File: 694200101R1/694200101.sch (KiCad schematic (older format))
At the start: 226 parts, among them J1 USB4085-GF-A, J2 Conn_01x02_Male, J3 Conn_01x02_Male, SW1 MX_SW, SW10 MX_SW, SW100 MX_SW, SW101 MX_SW, SW102 MX_SW, SW11 MX_SW, SW12 MX_SW, SW13 MX_SW, SW14 MX_SW, SW15 MX_SW, SW16 MX_SW, SW17 MX_SW, SW18 MX_SW, SW19 MX_SW, SW2 MX_SW, SW20 MX_SW, SW21 MX_SW, SW22 MX_SW, SW23 MX_SW, SW24 MX_SW, SW25 MX_SW, SW26 MX_SW, SW27 MX_SW, SW28 MX_SW, SW29 MX_SW, SW3 MX_SW, SW30 MX_SW, SW31 MX_SW, SW32 MX_SW, SW33 MX_SW, SW34 MX_SW, SW35 MX_SW, SW36 MX_SW, SW37 MX_SW, SW38 MX_SW, SW39 MX_SW, SW4 MX_SW, SW40 MX_SW, SW41 MX_SW, SW42 MX_SW, SW43 MX_SW, SW44 MX_SW, SW45 MX_SW, SW46 MX_SW, SW47 MX_SW, SW48 MX_SW, SW49 MX_SW, SW5 MX_SW, SW50 MX_SW, SW51 MX_SW, SW52 MX_SW, SW53 MX_SW, SW54 MX_SW, SW55 MX_SW, SW56 MX_SW, SW57 MX_SW, SW58 MX_SW, SW59 MX_SW, SW6 MX_SW, SW60 MX_SW, SW61 MX_SW, SW62 MX_SW, SW63 MX_SW, SW64 MX_SW, SW65 MX_SW, SW66 MX_SW, SW67 MX_SW, SW68 MX_SW, SW69 MX_SW, SW7 MX_SW, SW70 MX_SW, SW71 MX_SW, SW72 MX_SW, SW73 MX_SW, SW74 MX_SW, SW75 MX_SW, SW76 MX_SW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

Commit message: Added Missing Col_8
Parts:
- added D? (x5): LL4148, eec-fairchild:Fairchild_ON_Semiconductor-LL4148-0, symbol eec-fairchild:LL4148
- added SW? (x5): MX_SW, cldg:millmax-mxalps, symbol cldg:MX_SW
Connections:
- wire segments 567 -> 582
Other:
- moved on the sheet: D100, D101, D102, D103, D40, D41, D42, D43, D44, D45, D46, D47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

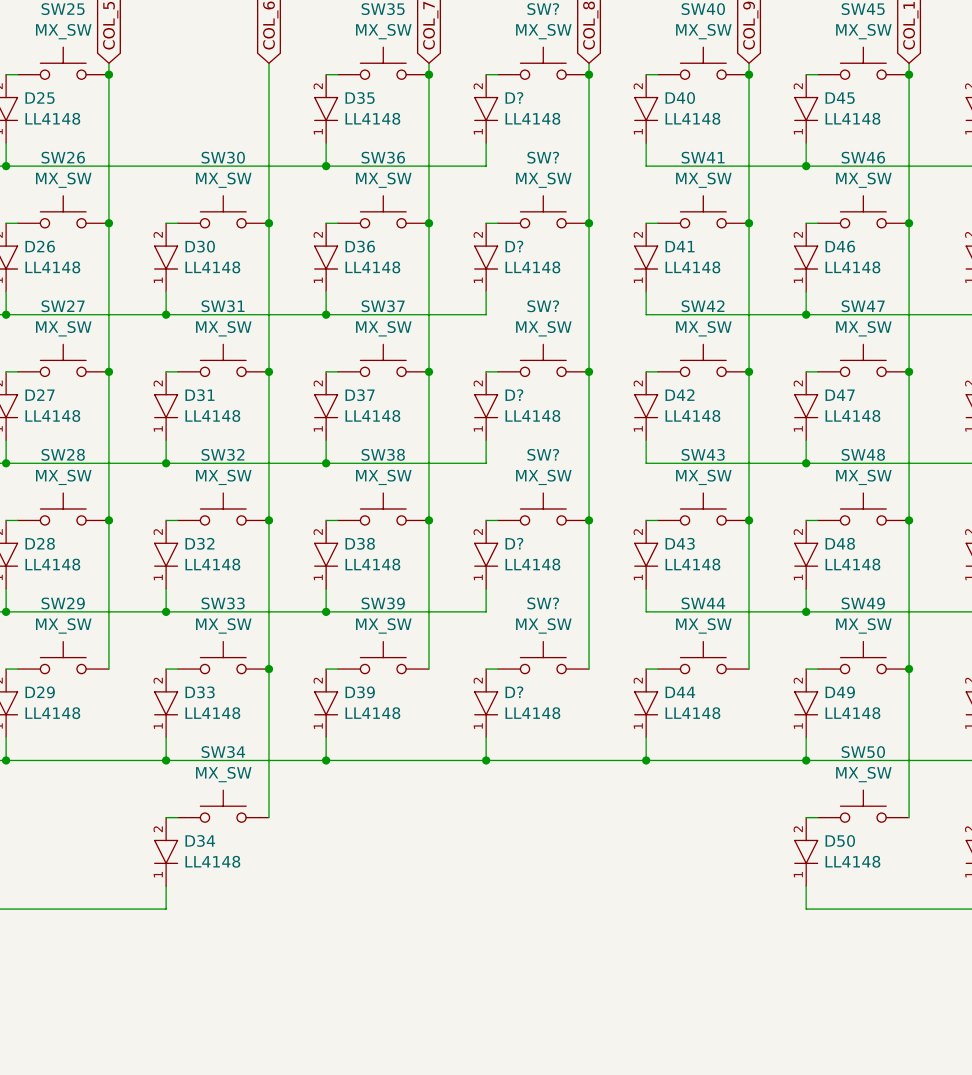
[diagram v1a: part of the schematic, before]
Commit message: Added Missing Wires
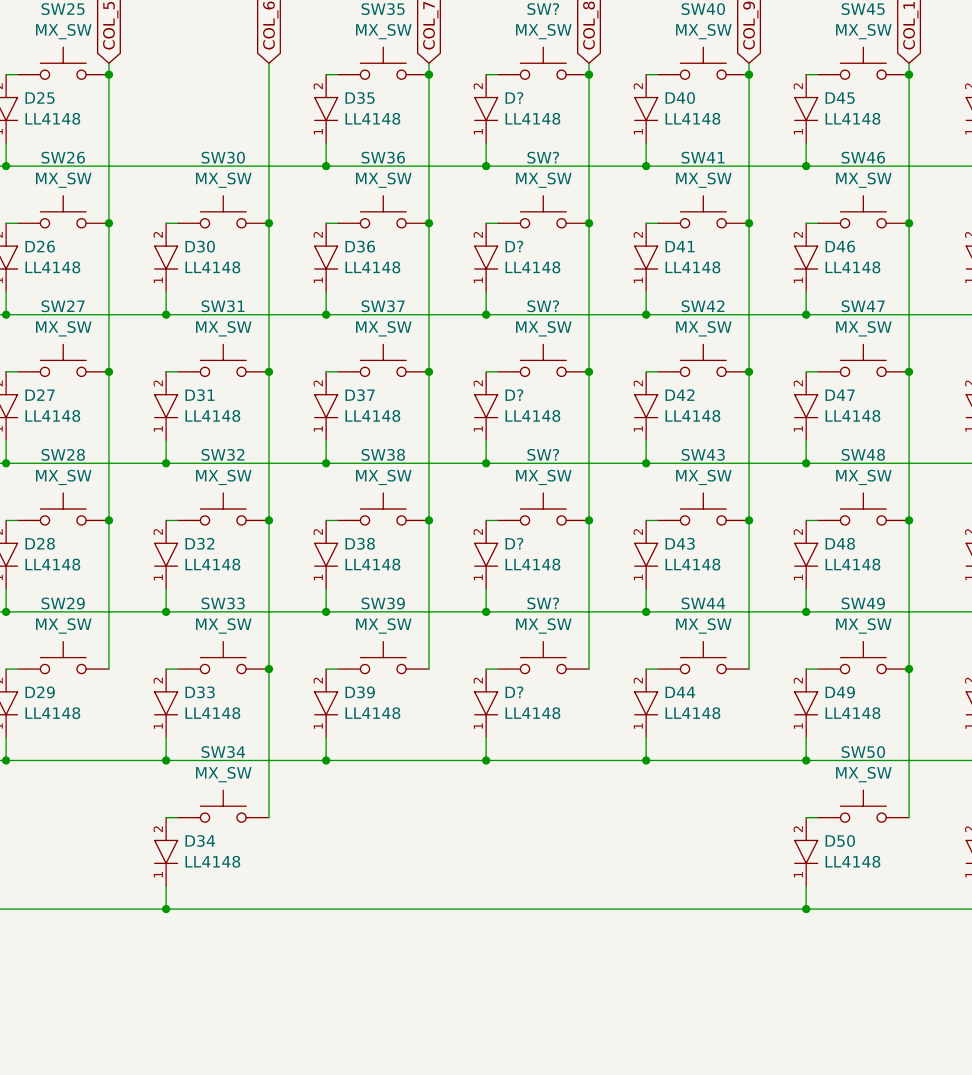
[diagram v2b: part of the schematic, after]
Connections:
- wire segments 582 -> 587
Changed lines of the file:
@@
 $EndComp
-Wire Wire Line
-	6350 1850 6350 1950
 Wire Wire Line
 	6400 1550 6350 1550
@@
 	6350 3900 7050 3900
 Connection ~ 7050 3900
+Wire Wire Line
+	4950 4550 7750 4550
+Connection ~ 4950 4550
+Connection ~ 7750 4550
+Wire Wire Line
+	6350 1300 7050 1300
+Connection ~ 6350 1300
+Connection ~ 7050 1300
+Wire Wire Line
+	6350 1850 6350 1950
+Wire Wire Line
+	6350 1950 7050 1950
+Connection ~ 6350 1950
+Connection ~ 7050 1950
+Wire Wire Line
+	6350 2600 7050 2600
+Connection ~ 6350 2600
+Connection ~ 7050 2600
+Wire Wire Line
+	6350 3250 7050 3250
+Connection ~ 6350 3250
+Connection ~ 7050 3250
 $EndSCHEMATC

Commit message: top row buttons
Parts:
- gave numbers to parts that had none: 10
- renumbered D95 to D100, D96 to D101, D97 to D102, D98 to D103, D99 to D104, D100 to D105, D101 to D106, D102 to D107, D103 to D108, D40 to D45, D41 to D46, D42 to D47, D43 to D48, D44 to D49, D45 to D50, D46 to D51, D47 to D52, D48 to D53, D49 to D54, D50 to D55, D51 to D56, D52 to D57, D53 to D58, D54 to D59, D55 to D60, D56 to D61, D57 to D62, D58 to D63, D59 to D64, D60 to D65, D61 to D66, D62 to D67, D63 to D68, D64 to D69, D65 to D70, D66 to D71, D67 to D72, D68 to D73, D69 to D74, D70 to D75, D71 to D76, D72 to D77, D73 to D78, D74 to D79, D75 to D80, D76 to D81, D77 to D82, D78 to D83, D79 to D84, D80 to D85, D81 to D86, D82 to D87, D83 to D88, D84 to D89, D85 to D90, D86 to D91, D87 to D92, D88 to D93, D89 to D95, D90 to D96, D91 to D97, D92 to D98, D93 to D99, SW95 to SW100, SW96 to SW101, SW97 to SW102, SW98 to SW103, SW99 to SW104, SW100 to SW105, SW101 to SW106, SW102 to SW107, SW40 to SW45, SW41 to SW46, SW42 to SW47, SW43 to SW48, SW44 to SW49, SW45 to SW50, SW46 to SW51, SW47 to SW52, SW48 to SW53, SW49 to SW54, SW50 to SW55, SW51 to SW56, SW52 to SW57, SW53 to SW58, SW54 to SW59, SW55 to SW60, SW56 to SW61, SW57 to SW62, SW58 to SW63, SW59 to SW64, SW60 to SW65, SW61 to SW66, SW62 to SW67, SW63 to SW68, SW64 to SW69, SW65 to SW70, SW66 to SW71, SW67 to SW72, SW68 to SW73, SW69 to SW74, SW70 to SW75, SW71 to SW76, SW72 to SW77, SW73 to SW78, SW74 to SW79, SW75 to SW80, SW76 to SW81, SW77 to SW82, SW78 to SW83, SW79 to SW84, SW80 to SW85, SW81 to SW86, SW82 to SW87, SW83 to SW88, SW84 to SW89, SW85 to SW90, SW86 to SW91, SW87 to SW92, SW88 to SW93, SW89 to SW94, SW90 to SW95, SW91 to SW96, SW92 to SW97, SW93 to SW98, SW94 to SW99

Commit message: Added New Encoder
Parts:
- removed ENC1: PEC11R-4220F-S0024, eec-Bourns:Bourns-PEC11R-4220F-S0024-0-0-0, symbol eec-Bourns:PEC11R-4220F-S0024
- added IC?: PEC11L-4115F-S0020, PEC11L4115FS0020, symbol SamacSys_Parts:PEC11L-4115F-S0020
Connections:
- wire segments 587 -> 592
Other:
- moved on the sheet: D94
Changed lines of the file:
@@
 	10000 7800 9550 7800
 Wire Wire Line
-	14900 7700 14800 7700
-Connection ~ 13500 7900
-Wire Wire Line
-	13500 7900 13600 7900
-Wire Wire Line
-	13500 7800 13600 7800
-Wire Wire Line
 	16050 6350 16050 6500
 Wire Wire Line
@@
 	15750 6350 16050 6350
 Wire Wire Line
-	14800 7300 15400 7300
+	14750 7300 15400 7300
 Wire Wire Line
 	16050 7400 16050 7300
 Wire Wire Line
-	14800 7400 16050 7400
+	14750 7400 16050 7400
 Wire Wire Line
 	15400 7300 15400 7500
@@
 Wire Wire Line
 	5400 850  5400 1550
-Wire Wire Line
-	13600 7200 13200 7200
-Text GLabel 13200 7200 0    50   Input ~ 0
+Text GLabel 13200 7250 0    50   Input ~ 0
 COL_22
 $Comp
-L eec-fairchild:LL4148 D94
-U 1 1 638FF624
-P 13650 7600
-F 0 "D94" V 13854 7678 50  0000 L CNN
-F 1 "LL4148" V 13945 7678 50  0000 L CNN
-F 2 "eec-fairchild:Fairchild_ON_Semiconductor-LL4148-0" H 13650 8000 50  0001 L CNN
-F 3 "https://www.fairchildsemi.com/datasheets/LL/LL4148.pdf" H 13650 8100 50  0001 L CNN
-F 4 "Diode" H 13650 8200 50  0001 L CNN "category"
-F 5 "DIODE GEN PURP 100V 200MA SOD80" H 13650 8300 50  0001 L CNN "digikey description"
-F 6 "LL4148FSCT-ND" H 13650 8400 50  0001 L CNN "digikey part number"
-F 7 "yes" H 13650 8500 50  0001 L CNN "lead free"
-F 8 "7267ed481d20a817" H 13650 8600 50  0001 L CNN "library id"
-F 9 "Fairchild/ON Semiconductor" H 13650 8700 50  0001 L CNN "manufacturer"
-F 10 "512-LL4148" H 13650 8800 50  0001 L CNN "mouser part number"
-F 11 "2" H 13650 8900 50  0001 L CNN "num pins"
-F 12 "SOD80" H 13650 9000 50  0001 L CNN "package"
-F 13 "yes" H 13650 9100 50  0001 L CNN "rohs"
-F 14 "+175°C" H 13650 9200 50  0001 L CNN "temperature range high"
-F 15 "-55°C" H 13650 9300 50  0001 L CNN "temperature range low"
-F 16 "" H 13650 9400 50  0001 L CNN "voltage"
-	1    13650 7600
-	-1   0    0    1
-$EndComp
-Wire Wire Line
-	13550 7600 13600 7600
-Text GLabel 13200 7600 0    50   Input ~ 0
-ROW_0
-Wire Wire Line
-	13200 7600 13250 7600
-Connection ~ 14900 8150
-Wire Wire Line
-	14900 8150 14900 8350
-Wire Wire Line
-	14900 8150 14900 7700
-Wire Wire Line
-	13500 7800 13500 7900
-$Comp
-L eec-Bourns:PEC11R-4220F-S0024 ENC1
-U 1 1 5FEA104E
-P 13500 7200
-F 0 "ENC1" H 14200 7465 50  0000 C CNN
-F 1 "PEC11R-4220F-S0024" H 14200 7374 50  0000 C CNN
-F 2 "eec-Bourns:Bourns-PEC11R-4220F-S0024-0-0-0" H 13500 7600 50  0001 L CNN
-F 3 "https://www.bourns.com/docs/product-datasheets/pec11r.pdf?sfvrsn=bb617cbf_6" H 13500 7700 50  0001 L CNN
-F 4 "Enc" H 13500 7800 50  0001 L CNN "category"
-F 5 "10mA" H 13500 7900 50  0001 L CNN "current rating"
-F 6 "Yes" H 13500 8000 50  0001 L CNN "detend"
-F 7 "Electromechanical" H 13500 8100 50  0001 L CNN "device class L1"
-F 8 "Switches" H 13500 8200 50  0001 L CNN "device class L2"
-F 9 "Encoders" H 13500 8300 50  0001 L CNN "device class L3"
-F 10 "ROTARY ENCODER MECHANICAL 24PPR" H 13500 8400 50  0001 L CNN "digikey description"
-F 11 "PEC11R-4220F-S0024-ND" H 13500 8500 50  0001 L CNN "digikey part number"
-F 12 "Incremental" H 13500 8600 50  0001 L CNN "encoder type"
-F 13 "27.3mm" H 13500 8700 50  0001 L CNN "height"
-F 14 "yes" H 13500 8800 50  0001 L CNN "lead free"
-F 15 "456a2eefc9d34d73" H 13500 8900 50  0001 L CNN "library id"
-F 16 "Bourns" H 13500 9000 50  0001 L CNN "manufacturer"
-F 17 "Encoders 20mm SHAFT w/SWITCH" H 13500 9100 50  0001 L CNN "mouser description"
-F 18 "652-PEC11R-4220F-S24" H 13500 9200 50  0001 L CNN "mouser part number"
-F 19 "1" H 13500 9300 50  0001 L CNN "number of circuits"
-F 20 "ENC_PTH_12MM5_13MM4" H 13500 9400 50  0001 L CNN "package"
-F 21 "24" H 13500 9500 50  0001 L CNN "pulses per rev"
-F 22 "yes" H 13500 9600 50  0001 L CNN "rohs"
-F 23 "+70°C" H 13500 9700 50  0001 L CNN "temperature range high"
-F 24 "30°C" H 13500 9800 50  0001 L CNN "temperature range low"
-F 25 "5V" H 13500 9900 50  0001 L CNN "voltage rating DC"
-	1    13500 7200
-	1    0    0    -1
-$EndComp
-Connection ~ 13500 8150
-$Comp
 L power:GND #PWR010
 U 1 1 5FEB2ECC
-P 13500 8150
-F 0 "#PWR010" H 13500 7900 50  0001 C CNN
-F 1 "GND" H 13505 7977 50  0000 C CNN
-F 2 "" H 13500 8150 50  0001 C CNN
-F 3 "" H 13500 8150 50  0001 C CNN
-	1    13500 8150
+P 14100 7900
+F 0 "#PWR010" H 14100 7650 50  0001 C CNN
+F 1 "GND" H 14105 7727 50  0000 C CNN
+F 2 "" H 14100 7900 50  0001 C CNN
+F 3 "" H 14100 7900 50  0001 C CNN
+	1    14100 7900
 	1    0    0    -1
 $EndComp
 Wire Wire Line
-	13500 8150 14900 8150
-Wire Wire Line
-	13500 7900 13500 8150
-Wire Wire Line
 	13900 5950 13800 5950
 Wire Wire Line
@@
 Connection ~ 6350 3250
 Connection ~ 7050 3250
+Wire Wire Line
+	13600 7250 13200 7250
+$Comp
+L SamacSys_Parts:PEC11L-4115F-S0020 IC?
+U 1 1 5FF3C341
+P 14100 6850
+F 0 "IC?" V 13919 6850 50  0000 C CNN
+F 1 "PEC11L-4115F-S0020" V 14010 6850 50  0000 C CNN
+F 2 "PEC11L4115FS0020" H 14950 7150 50  0001 L CNN
+F 3 "" H 14950 7050 50  0001 L CNN
+F 4 "Encoders ENCODER" H 14950 6950 50  0001 L CNN "Description"
+F 5 "25" H 14950 6850 50  0001 L CNN "Height"
+F 6 "652-PEC11L4115FS0020" H 14950 6750 50  0001 L CNN "Mouser Part Number"
+F 7 "https://www.mouser.co.uk/ProductDetail/Bourns/PEC11L-4115F-S0020?qs=gk21WLQFtgRAgrgJZfpkWw%3D%3D" H 14950 6650 50  0001 L CNN "Mouser Price/Stock"
+F 8 "Bourns" H 14950 6550 50  0001 L CNN "Manufacturer_Name"
+F 9 "PEC11L-4115F-S0020" H 14950 6450 50  0001 L CNN "Manufacturer_Part_Number"
+	1    14100 6850
+	0    -1   1    0
+$EndComp
+Wire Wire Line
+	13200 7350 13250 7350
+Text GLabel 13200 7350 0    50   Input ~ 0
+ROW_0
+Wire Wire Line
+	13550 7350 13600 7350
+$Comp
+L eec-fairchild:LL4148 D94
+U 1 1 638FF624
+P 13650 7350
+F 0 "D94" V 13854 7428 50  0000 L CNN
+F 1 "LL4148" V 13945 7428 50  0000 L CNN
+F 2 "eec-fairchild:Fairchild_ON_Semiconductor-LL4148-0" H 13650 7750 50  0001 L CNN
+F 3 "https://www.fairchildsemi.com/datasheets/LL/LL4148.pdf" H 13650 7850 50  0001 L CNN
+F 4 "Diode" H 13650 7950 50  0001 L CNN "category"
+F 5 "DIODE GEN PURP 100V 200MA SOD80" H 13650 8050 50  0001 L CNN "digikey description"
+F 6 "LL4148FSCT-ND" H 13650 8150 50  0001 L CNN "digikey part number"
+F 7 "yes" H 13650 8250 50  0001 L CNN "lead free"
+F 8 "7267ed481d20a817" H 13650 8350 50  0001 L CNN "library id"
+F 9 "Fairchild/ON Semiconductor" H 13650 8450 50  0001 L CNN "manufacturer"
+F 10 "512-LL4148" H 13650 8550 50  0001 L CNN "mouser part number"
+F 11 "2" H 13650 8650 50  0001 L CNN "num pins"
+F 12 "SOD80" H 13650 8750 50  0001 L CNN "package"
+F 13 "yes" H 13650 8850 50  0001 L CNN "rohs"
+F 14 "+175°C" H 13650 8950 50  0001 L CNN "temperature range high"
+F 15 "-55°C" H 13650 9050 50  0001 L CNN "temperature range low"
+F 16 "" H 13650 9150 50  0001 L CNN "voltage"
+	1    13650 7350
+	-1   0    0    1
+$EndComp
+Wire Wire Line
+	14750 7300 14750 7250
+Wire Wire Line
+	14750 7250 14600 7250
+Wire Wire Line
+	14750 7400 14750 7450
+Wire Wire Line
+	14750 7450 14600 7450
+Wire Wire Line
+	14100 6800 14650 6800
+Wire Wire Line
+	14650 6800 14650 7350
+Wire Wire Line
+	14650 7350 14600 7350
+Wire Wire Line
+	14650 7350 14650 7900
+Wire Wire Line
+	14650 7900 14100 7900
+Wire Wire Line
+	14100 7900 14100 7850
+Connection ~ 14650 7350
+Connection ~ 14100 7900
+Wire Wire Line
+	14900 7900 14900 8350
+Wire Wire Line
+	14650 7900 14900 7900
+Connection ~ 14650 7900
+Wire Wire Line
+	14100 6800 14100 6850
 $EndSCHEMATC

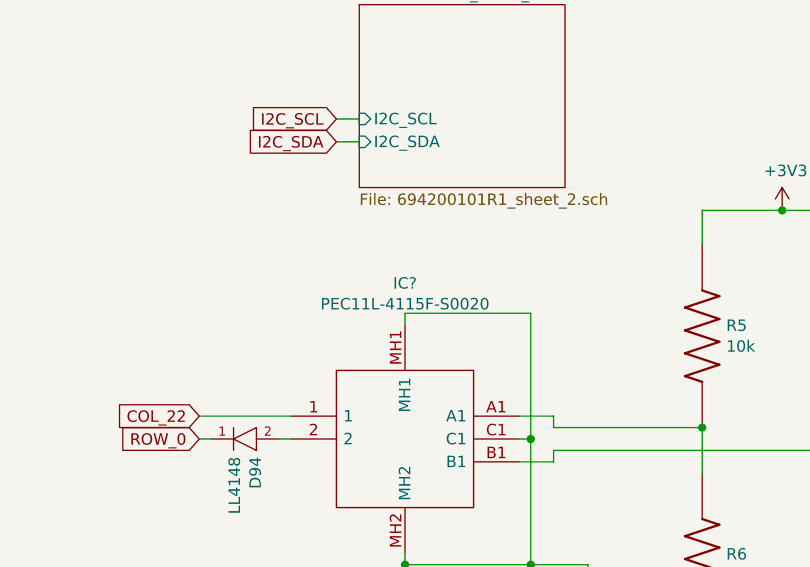
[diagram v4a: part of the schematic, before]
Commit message: update enc footprint
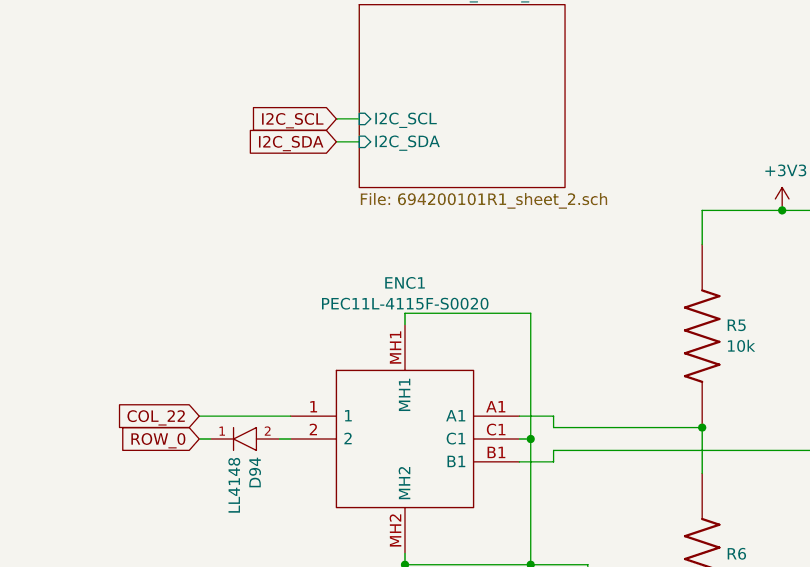
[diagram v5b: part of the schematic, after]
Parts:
- gave numbers to parts that had none: 1
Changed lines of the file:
@@
 	13600 7250 13200 7250
 $Comp
-L SamacSys_Parts:PEC11L-4115F-S0020 IC?
+L SamacSys_Parts:PEC11L-4115F-S0020 ENC1
 U 1 1 5FF3C341
 P 14100 6850
-F 0 "IC?" V 13919 6850 50  0000 C CNN
+F 0 "ENC1" V 13919 6850 50  0000 C CNN
 F 1 "PEC11L-4115F-S0020" V 14010 6850 50  0000 C CNN
 F 2 "PEC11L4115FS0020" H 14950 7150 50  0001 L CNN

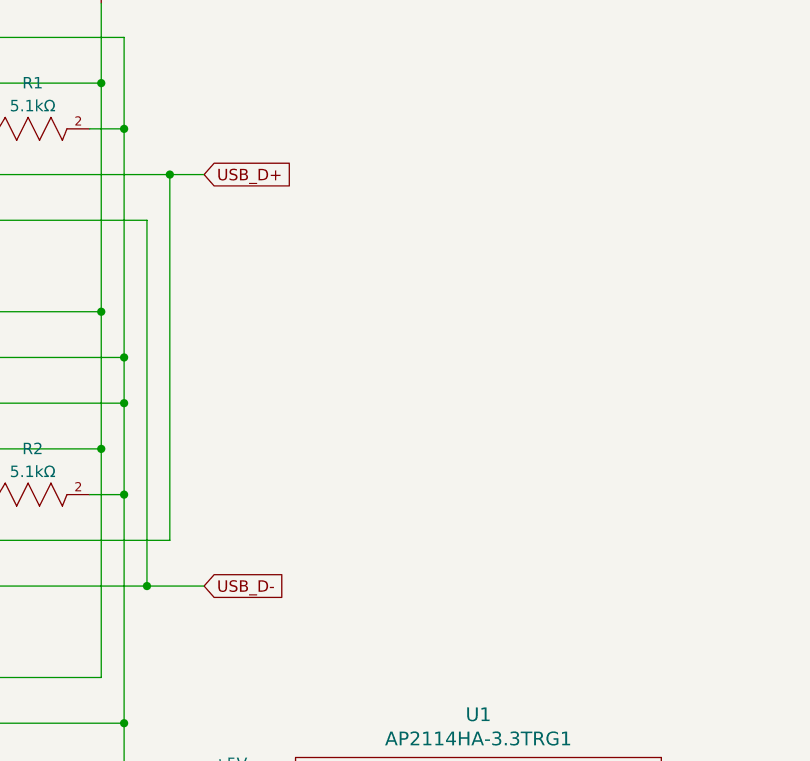
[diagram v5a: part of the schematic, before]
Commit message: added usb ESD
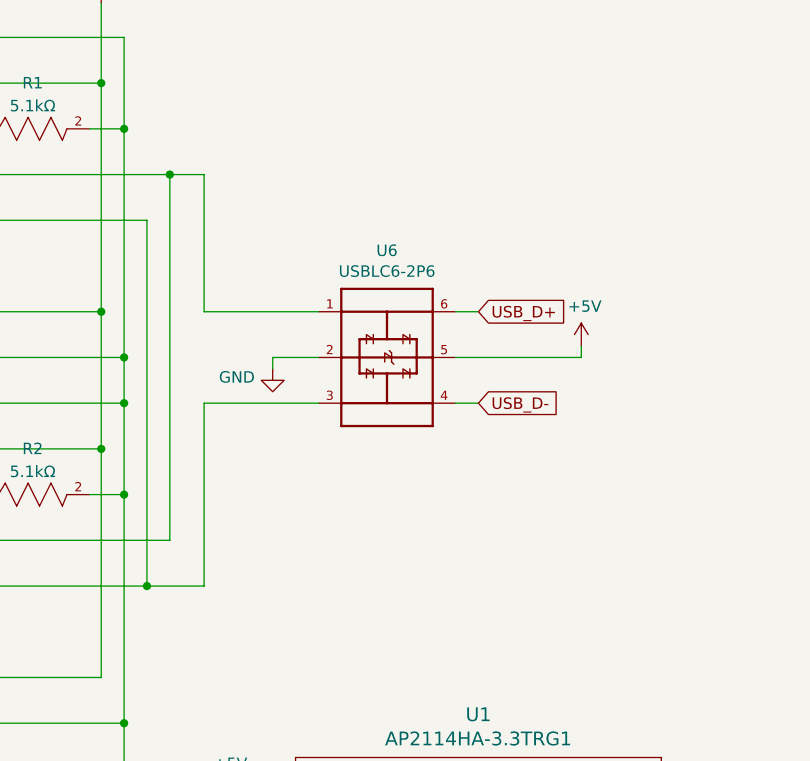
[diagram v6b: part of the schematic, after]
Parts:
- added U6: USBLC6-2P6, SOT50P160X60-6N, symbol cldg:USBLC6-2P6
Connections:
- net +5V: now also U6.5
- net GND: now also U6.2
- net USB_D+: now also U6.6; no longer J1.A6 (Dp1), J1.B6 (Dp2)
- net USB_D-: now also U6.4; no longer J1.A7 (Dn1), J1.B7 (Dn2)
- new net: J1.A6 (Dp1), J1.B6 (Dp2), U6.1
- new net: J1.A7 (Dn1), J1.B7 (Dn2), U6.3
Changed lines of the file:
@@
 Wire Wire Line
 	2400 7950 2400 8950
-Text GLabel 2850 6750 2    50   Input ~ 0
+Text GLabel 4050 7350 2    50   Input ~ 0
 USB_D+
-Text GLabel 2850 8550 2    50   Input ~ 0
+Text GLabel 4050 7750 2    50   Input ~ 0
 USB_D-
 Connection ~ 2400 6350
@@
 Wire Wire Line
 	14100 6800 14100 6850
+$Comp
+L cldg:USBLC6-2P6 U6
+U 1 1 5FF3E6C9
+P 3650 7550
+F 0 "U6" H 3650 8017 50  0000 C CNN
+F 1 "USBLC6-2P6" H 3650 7926 50  0000 C CNN
+F 2 "SOT50P160X60-6N" H 3650 7550 50  0001 L BNN
+F 3 "" H 3650 7550 50  0001 L BNN
+F 4 "ST MICROELECTRONICS" H 3650 7550 50  0001 L BNN "MANUFACTURER"
+F 5 "SOT-666" H 3650 7550 50  0001 L BNN "PACKAGE"
+F 6 "5" H 3650 7550 50  0001 L BNN "PARTREV"
+F 7 "IPC 7351B" H 3650 7550 50  0001 L BNN "STANDARD"
+	1    3650 7550
+	1    0    0    -1
+$EndComp
+$Comp
+L power:+5V #PWR?
+U 1 1 600F480E
+P 4500 7500
+F 0 "#PWR?" H 4500 7350 50  0001 C CNN
+F 1 "+5V" H 4515 7673 50  0000 C CNN
+F 2 "" H 4500 7500 50  0001 C CNN
+F 3 "" H 4500 7500 50  0001 C CNN
+	1    4500 7500
+	1    0    0    -1
+$EndComp
+Wire Wire Line
+	3350 7350 2850 7350
+Wire Wire Line
+	2850 7350 2850 6750
+Wire Wire Line
+	3350 7750 2850 7750
+Wire Wire Line
+	2850 7750 2850 8550
+$Comp
+L power:GND #PWR?
+U 1 1 604813CB
+P 3150 7600
+F 0 "#PWR?" H 3150 7350 50  0001 C CNN
+F 1 "GND" H 3072 7563 50  0000 R CNN
+F 2 "" H 3150 7600 50  0001 C CNN
+F 3 "" H 3150 7600 50  0001 C CNN
+	1    3150 7600
+	1    0    0    -1
+$EndComp
+Wire Wire Line
+	4050 7350 3950 7350
+Wire Wire Line
+	3950 7750 4050 7750
+Wire Wire Line
+	3350 7550 3150 7550
+Wire Wire Line
+	3150 7550 3150 7600
+Wire Wire Line
+	3950 7550 4500 7550
+Wire Wire Line
+	4500 7550 4500 7500
 $EndSCHEMATC
